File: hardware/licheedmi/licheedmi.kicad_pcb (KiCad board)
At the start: 4 copper layers, 94 x 38 mm, 65 parts, among them J1 Conn_01x09, J2 HDMI_A_PCB, J3 LicheePiNano_LCD, J4 HDMI_A, U1 TDA19988, U2 LicheeNano, U3 TS3DV20812, U4 SC6206B

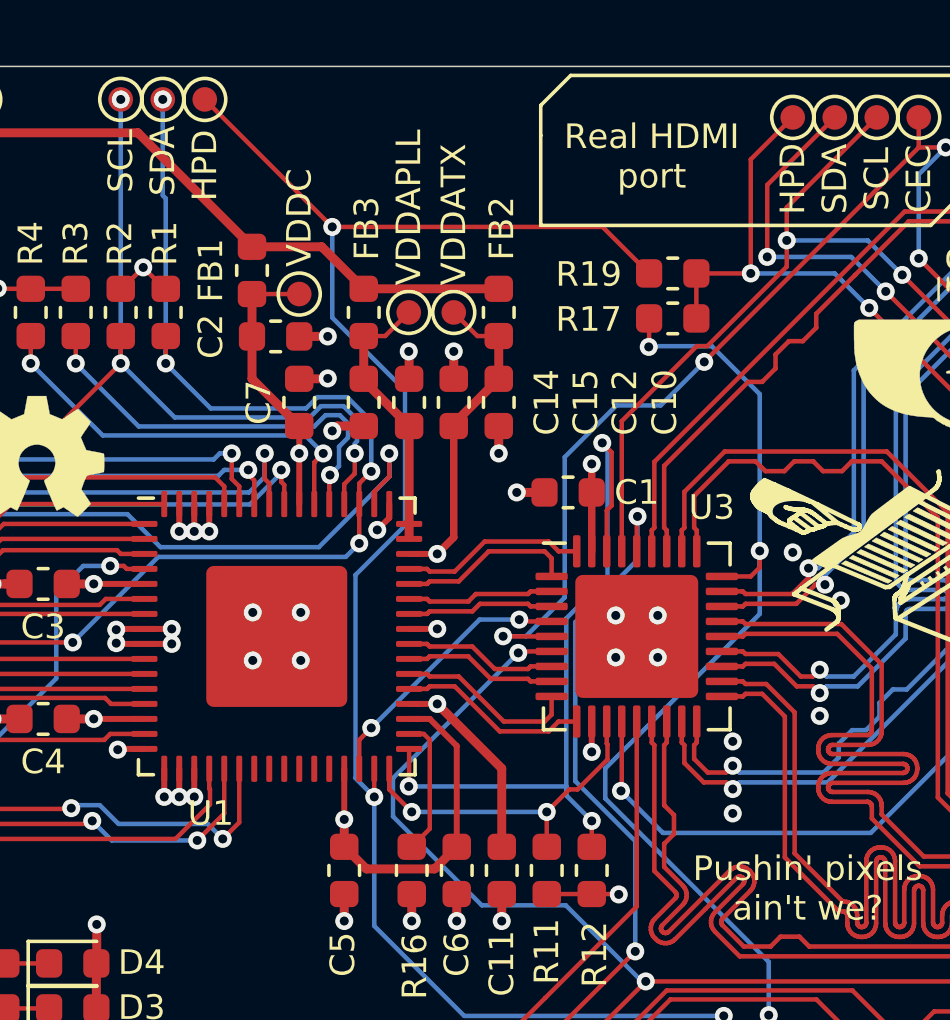
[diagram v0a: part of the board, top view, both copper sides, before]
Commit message: pcb: Fix silk for testpads
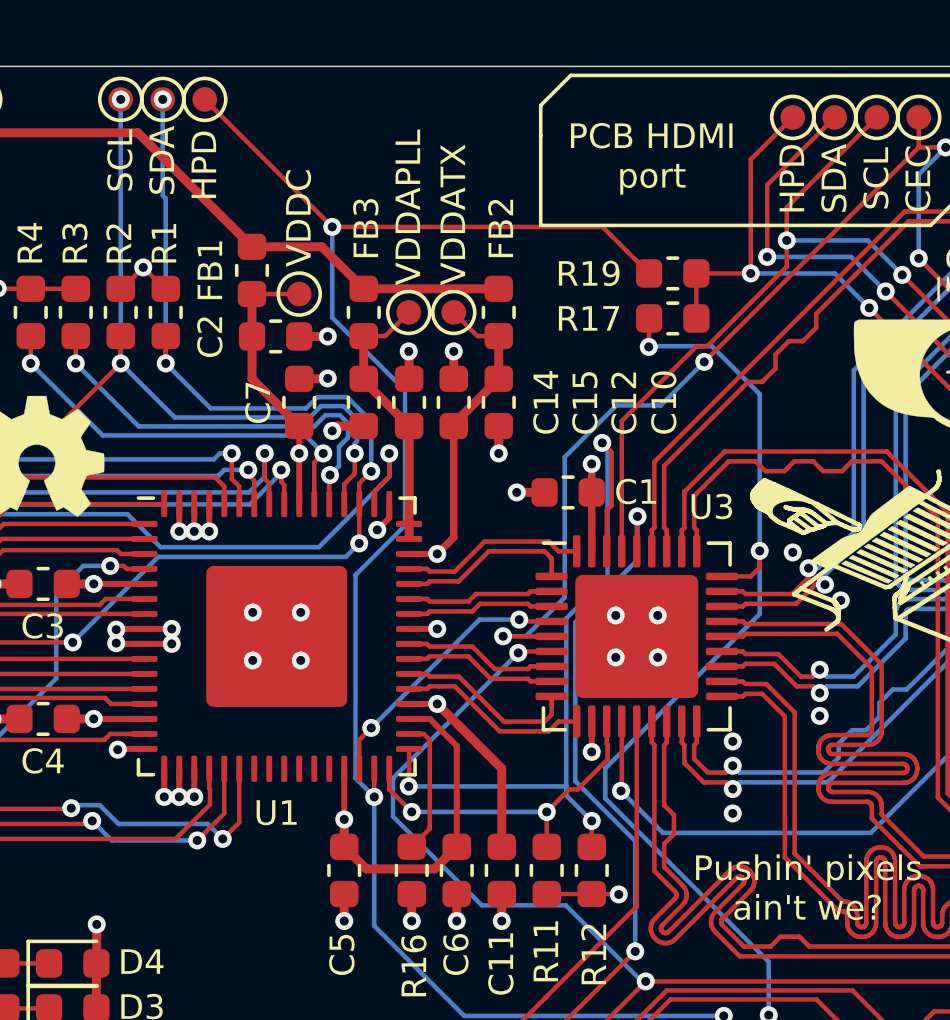
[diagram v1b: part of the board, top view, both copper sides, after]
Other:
- board text added: "PCB HDMI port"
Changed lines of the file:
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@@
     (tags "QFN DFN_QFN")
     (attr smd)
-    (fp_text reference U1 (at -2.2 5.9) (layer F.SilkS)
+    (fp_text reference U1 (at 0 5.9) (layer F.SilkS)
       (effects (font (size 0.82 0.82) (thickness 0.15)))
     )
@@
   (gr_arc (start 167 107) (end 167 109) (angle -90) (layer Edge.Cuts) (width 0.05))
   (gr_arc (start 77 107) (end 75 107) (angle -90) (layer Edge.Cuts) (width 0.05))
-  (gr_text "Real HDMI\nport" (at 145.5 74) (layer F.SilkS)
+  (gr_text "PCB HDMI\nport" (at 145.5 74) (layer F.SilkS)
     (effects (font (size 0.82 0.82) (thickness 0.15)))
   )

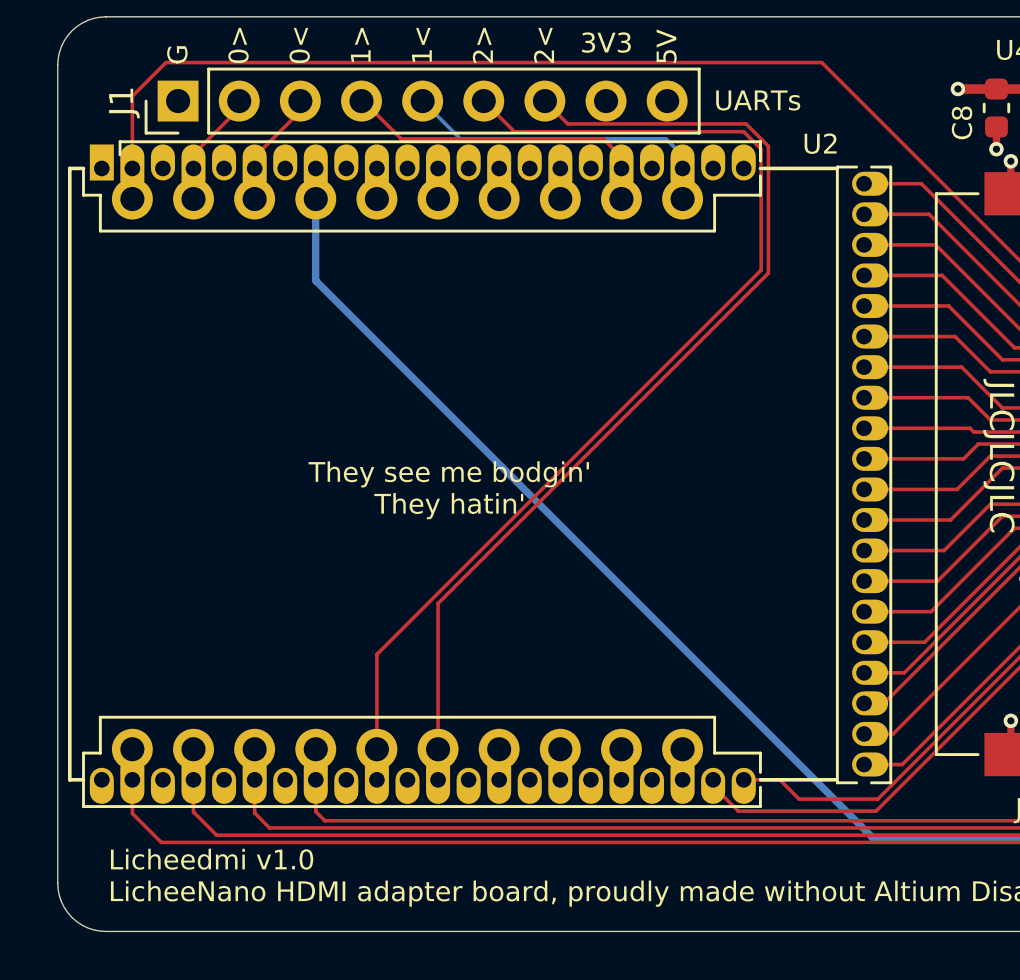
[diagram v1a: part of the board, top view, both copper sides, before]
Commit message: *: Add USB-UART chip (CH340C)
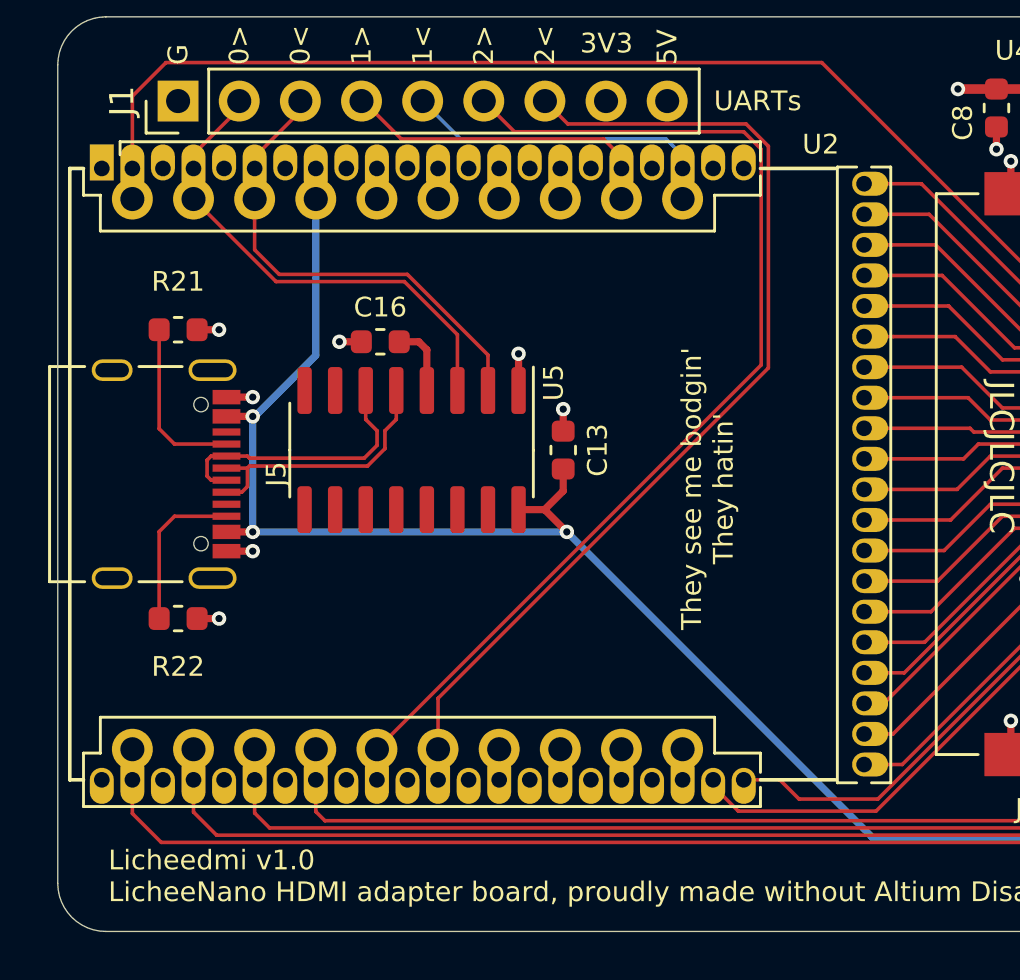
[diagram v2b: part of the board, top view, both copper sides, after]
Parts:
- added C13: 100n, Capacitor_SMD:C_0603_1608Metric, F.Cu at (96.0, 89.0)
- added C16: 100n, Capacitor_SMD:C_0603_1608Metric, F.Cu at (88.4, 84.5)
- added J5: USB_C_Receptacle_USB2.0, hdmizness:USB_C_Receptacle_Palconn_UTC16-G, F.Cu at (79.5, 90.0)
- added R21: 5k1, Resistor_SMD:R_0603_1608Metric, F.Cu at (80.0, 84.0)
- added R22: 5k1, Resistor_SMD:R_0603_1608Metric, F.Cu at (80.0, 96.0)
- added U5: CH340C, Package_SO:SOIC-16_3.9x9.9mm_P1.27mm, F.Cu at (89.7, 89.0)
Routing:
- net +5V: track 136.3 -> 152.7 mm, vias 2 -> 5
- net /TX0: track 3.59 -> 19.2 mm
- net /RX0: track 3.59 -> 18.7 mm
- net /USB_N: track 0.00 -> 11.4 mm
- net /USB_P: track 0.00 -> 11.3 mm
- net GND: track 74.7 -> 82.0 mm, vias 58 -> 65
- net Net-(J5-PadA5): track 0.00 -> 7.17 mm
- net Net-(J5-PadB5): track 0.00 -> 6.67 mm
- net Net-(C16-Pad2): track 0.00 -> 2.98 mm

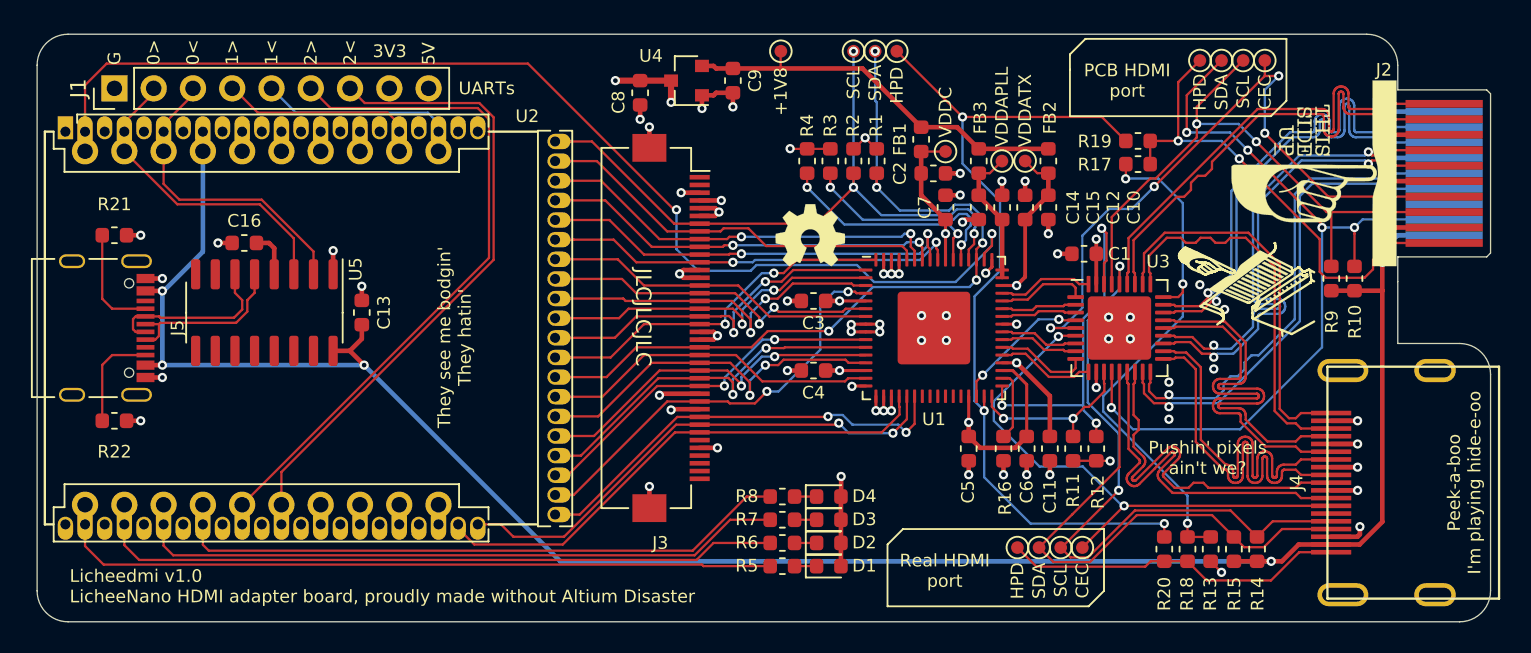
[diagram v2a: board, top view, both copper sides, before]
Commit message: sch, pcb: Add UART0 activity LEDs
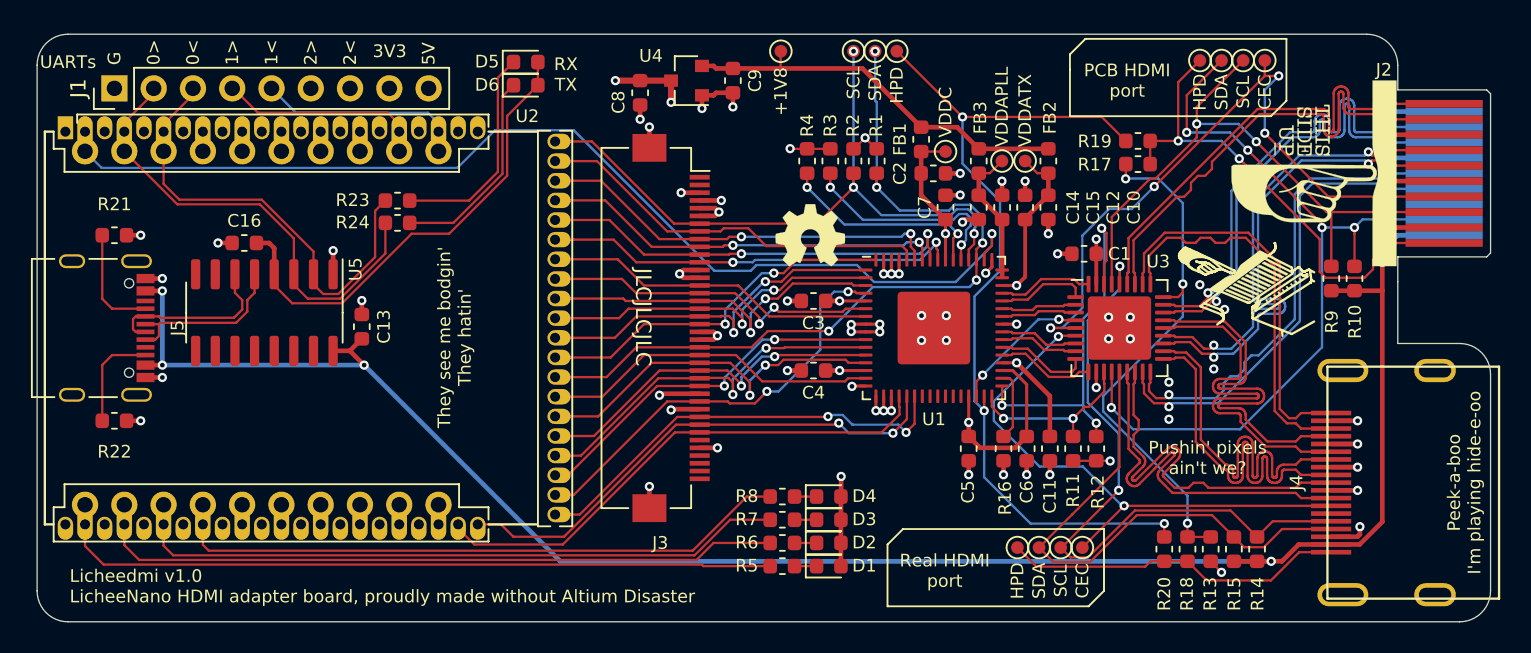
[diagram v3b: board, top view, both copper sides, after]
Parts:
- added D5: RED, LED_SMD:LED_0603_1608Metric, F.Cu at (106.6, 72.8)
- added D6: RED, LED_SMD:LED_0603_1608Metric, F.Cu at (106.6, 74.3)
- added R23: 1k, Resistor_SMD:R_0603_1608Metric, F.Cu at (98.3, 81.8)
- added R24: 1k, Resistor_SMD:R_0603_1608Metric, F.Cu at (98.3, 83.2)
- moved C13 0.91 mm to (96.0, 89.9)
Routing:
- net Net-(C16-Pad2): track 2.98 -> 30.8 mm
- net Net-(D5-Pad1): track 0.00 -> 14.0 mm
- net Net-(D6-Pad1): track 0.00 -> 13.3 mm
- net /TX0: track 19.2 -> 29.4 mm
- net /RX0: track 18.7 -> 28.5 mm
- net /HDMI_INT: track 73.5 -> 68.1 mm, vias 2 -> 1
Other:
- board text added: "RX TX"

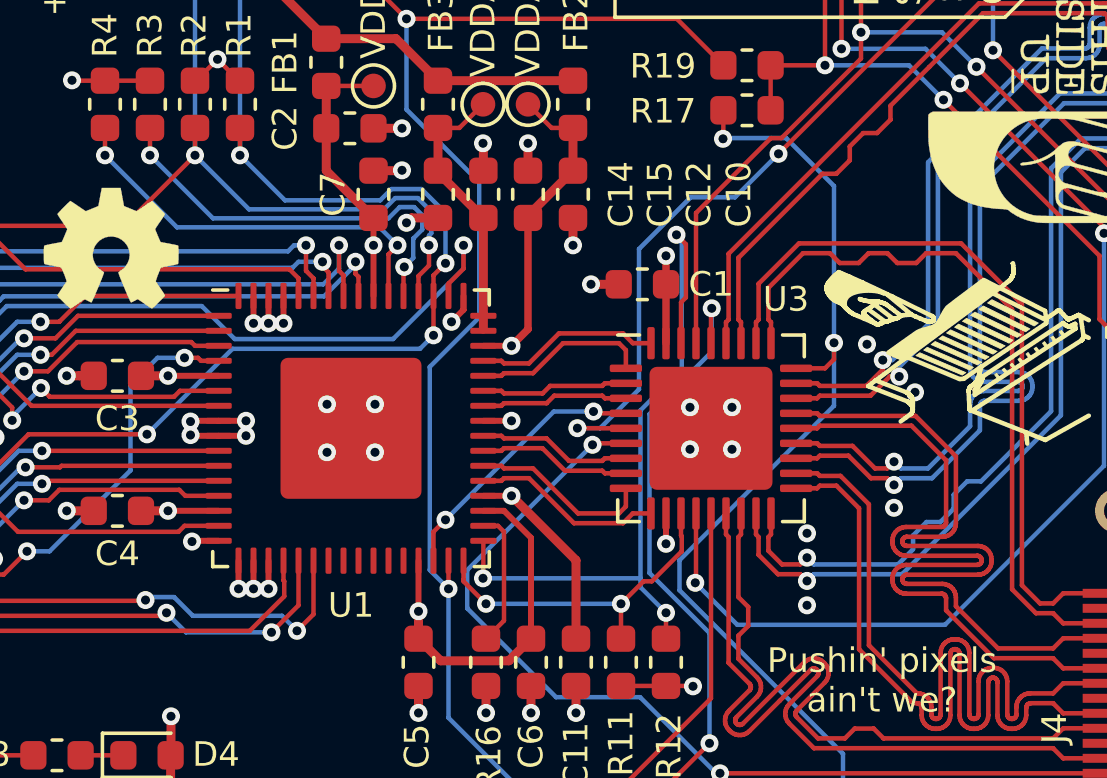
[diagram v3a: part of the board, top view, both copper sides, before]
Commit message: pcb: Fix DRC issues
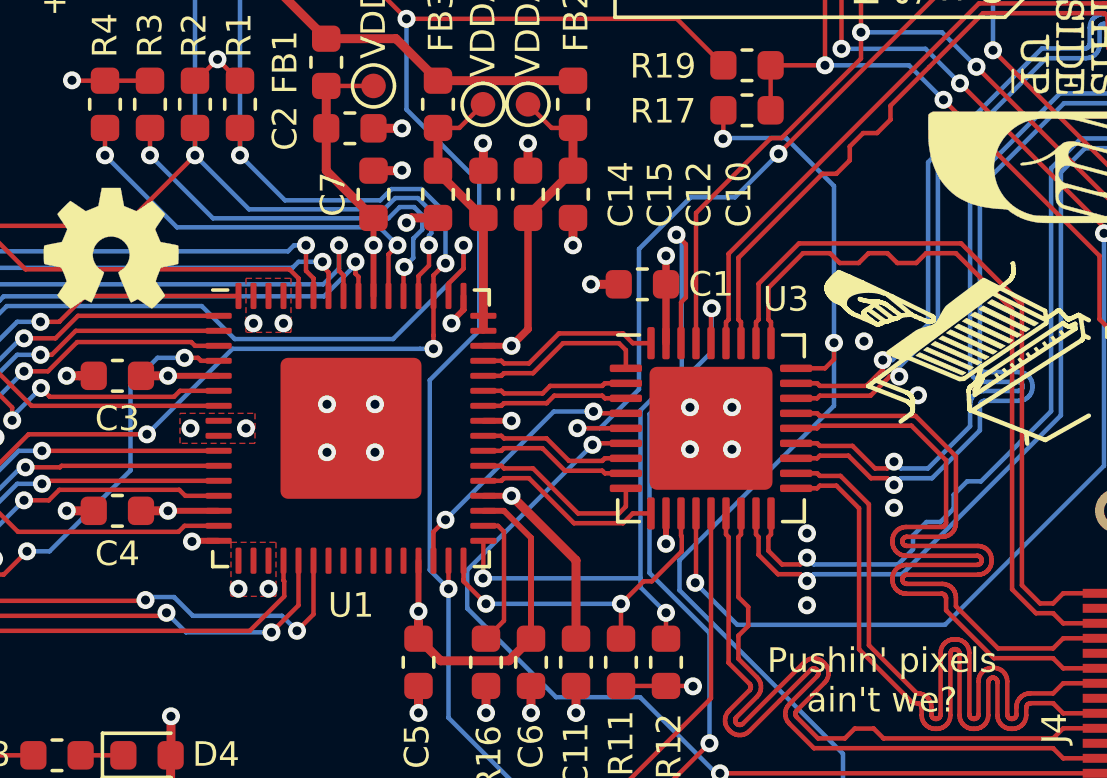
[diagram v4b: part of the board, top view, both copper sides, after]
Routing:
- net GND: track 82.0 -> 72.8 mm, vias 65 -> 61
- added copper zone on F.Cu, net GND

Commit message: Add FPC connector 3D model
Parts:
- J3: footprint Connector_FFC-FPC:Hirose_FH12-40S-0.5SH_1x40-1MP_P0.50mm_Horizontal -> hdmizness:Hirose_FH12-40S-0.5SH_1x40-1MP_P0.50mm_Horizontal
